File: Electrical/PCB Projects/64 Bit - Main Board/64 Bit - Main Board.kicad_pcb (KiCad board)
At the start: 4 copper layers, 200 x 100 mm, 242 parts, among them J1 61301021821, J10 M20-7920242R, J11 M20-7920242R, J12 M20-7920242R, J13 M20-7920242R, J14 1985195, J15 Conn_01x09, J16 Conn_01x09, J17 M20-7920242R, J18 M20-7920242R, J2 61301021821, J3 61301021821, J4 M20-7920242R, J5 USBC, J6 M20-7920242R, J7 PJ-102A, J8 M20-7920242R, J9 M20-7920242R, K1 JS-12N-K, K2 JS-12N-K, K3 JS-12N-K, K4 PR30-5V-450-1A-E, K5 PR30-12V-450-1A-E, P1 Conn_01x02, Q1 2N7002, Q10 XP231P0201TR-G, Q11 2N7002, Q2 XP231P0201TR-G, Q3 2N7002, Q4 2N7002, Q5 2N7002, Q6 XP231P0201TR-G, Q7 XP231P0201TR-G, Q8 2N7002, Q9 2N7002, SW1 1985195, SW2 1985195, SW3 1985195, SW4 1985195, SW5 L102011MS02Q, SW6 power_switch, U1 STM32F446RETx, U2 PCA9306, U3 DS1307+, U4 74HC3G34DC, U5 74HC3G34DC, U6 74HC3G34DC, U7 EN12-VS20AF20, U8 24LC64, U9 ESP32-C6-LCD-1.47, Y1 Crystal_GND24, Y2 32.768kHz-12.6pF, Y3 32.768kHz-12.6pF

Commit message: small pcb layout work
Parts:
- D47: moved to B.Cu
- moved JP1 67.8 mm to (191.9, 106.9), turned to -90 degrees
- moved D47 55.7 mm to (187.3, 103.5), turned to 180 degrees
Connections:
- D47 pad 2: Net-(D47-A) -> +5V
- JP1 pad 1: Net-(D47-A) -> Net-(JP1-A)
- JP1 pad 2: +5V -> Net-(D47-K)
- U9 pad 1: Net-(D47-K) -> Net-(JP1-A)
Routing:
- net encoder_button: track 196.4 -> 103.3 mm
- net encoder_A: track 215.8 -> 123.4 mm
- net encoder_B: track 227.6 -> 136.2 mm
- net +3V3: track 184.3 -> 103.8 mm, vias 17 -> 16
- net USART3_TX: track 164.4 -> 84.0 mm, vias 1 -> 0
- net IO9: track 152.6 -> 85.5 mm, vias 1 -> 0
- net USART3_RX: track 152.6 -> 86.8 mm, vias 1 -> 0
- net IO8: track 148.3 -> 84.8 mm
- net IO7: track 149.1 -> 86.8 mm
- net IO6: track 150.9 -> 89.0 mm
- net (no net): track 24.8 -> 0.00 mm
- net hv_output_relay: track 45.4 -> 32.0 mm
- net GND: vias 355 -> 332
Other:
- board text removed: "3v3"
- board text removed: "BL"
- board text removed: "CS"
- board text removed: "DC"
- board text removed: "MOSI"
- board text removed: "RST"
- board text removed: "SCK"
- board text removed: "SPI LCD"
- board text removed: "bottom"

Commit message: finished routing - added photoresistor to analog pin. Updated STM32Cube setup. Final stages of hardware design
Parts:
- removed D44, D45: TVS_0603, Resistor_SMD:R_0603_1608Metric
- removed the TP1 at (133.1, 160.6)
- removed the TP2 at (133.1, 164.1)
- removed the TP3 at (136.7, 160.6)
- removed the TP4 at (136.7, 164.1)
- removed the TP5 at (140.2, 160.6)
- removed the TP6 at (140.2, 164.1)
- added R80: R_Photo, OptoDevice:R_LDR_5.1x4.3mm_P3.4mm_Vertical, F.Cu at (76.5, 127.2)
- added R81: 10kohm_0603, Resistor_SMD:R_0603_1608Metric, F.Cu at (76.6, 121.0)
- D34, D35, D36, D37, D38, D39, D40, D41, D42, D43, D46, R76, R77, R78, R79: moved to B.Cu
- moved D36 134.5 mm to (84.2, 46.2), turned to 180 degrees
- moved D38 132.1 mm to (62.3, 74.7)
- moved D37 127.6 mm to (63.4, 78.1)
- moved D46 83.8 mm to (95.0, 122.5), turned to 90 degrees
- moved D43 75.5 mm to (94.8, 136.3), turned to 180 degrees
- moved D41 54.9 mm to (119.8, 133.9)
- moved D40 54.5 mm to (119.8, 132.1)
- moved D39 51.0 mm to (119.8, 135.7)
- moved R78 49.6 mm to (196.9, 134.7), turned to -90 degrees
- moved R79 49.0 mm to (193.9, 134.7), turned to -90 degrees
- moved R77 46.9 mm to (195.4, 134.7), turned to -90 degrees
- moved D35 45.9 mm to (196.2, 132.4), turned to 180 degrees
- moved D42 43.9 mm to (129.8, 132.0), turned to 90 degrees
- moved R76 43.0 mm to (192.4, 134.7), turned to -90 degrees
- moved D34 41.9 mm to (193.1, 132.4)
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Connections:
- U1 pad 8: unconnected-(U1-PC0-Pad8) -> photoResistor
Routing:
- net encoder_button: track 103.3 -> 201.7 mm
- net encoder_A: track 123.4 -> 221.0 mm
- net encoder_B: track 136.2 -> 232.4 mm
- net +3V3: track 103.8 -> 188.9 mm, vias 16 -> 17
- net USART3_TX: track 84.0 -> 147.7 mm, vias 0 -> 1
- net USART3_RX: track 86.8 -> 150.2 mm, vias 0 -> 1
- net +3V3_2: track 188.5 -> 224.2 mm
- net IO6: track 89.0 -> 66.2 mm, vias 0 -> 1
- net photoResistor: track 0.00 -> 18.3 mm, vias 0 -> 1
- net IO7: track 86.8 -> 70.4 mm, vias 0 -> 1
- net IO9: track 85.5 -> 101.2 mm, vias 0 -> 1
- net hv_output_relay: track 32.0 -> 45.4 mm
- net IO8: track 84.8 -> 72.2 mm, vias 0 -> 1
- net GND: track 160.1 -> 171.4 mm, vias 332 -> 520
- net +5V: track 405.6 -> 416.1 mm, vias 23 -> 24
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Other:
- board text added: "'64 Bit' Nixie Tube Clock Driver Board_V1.0 Nov 2025"
- board text removed: "'64 Bit' Nixie Tube Clock Driver Board_V1.0 Oct 2025"
- board text removed: "top"

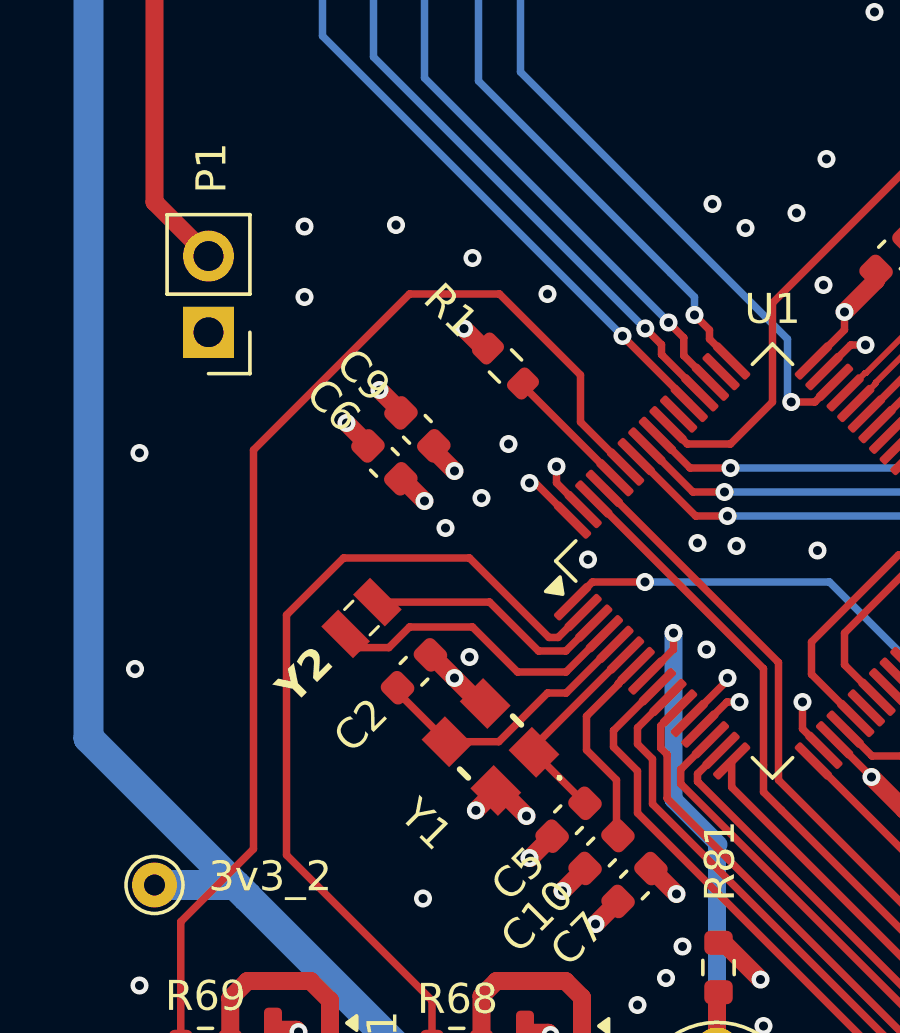
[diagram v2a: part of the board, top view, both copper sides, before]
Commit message: added I2C ambient light sensor
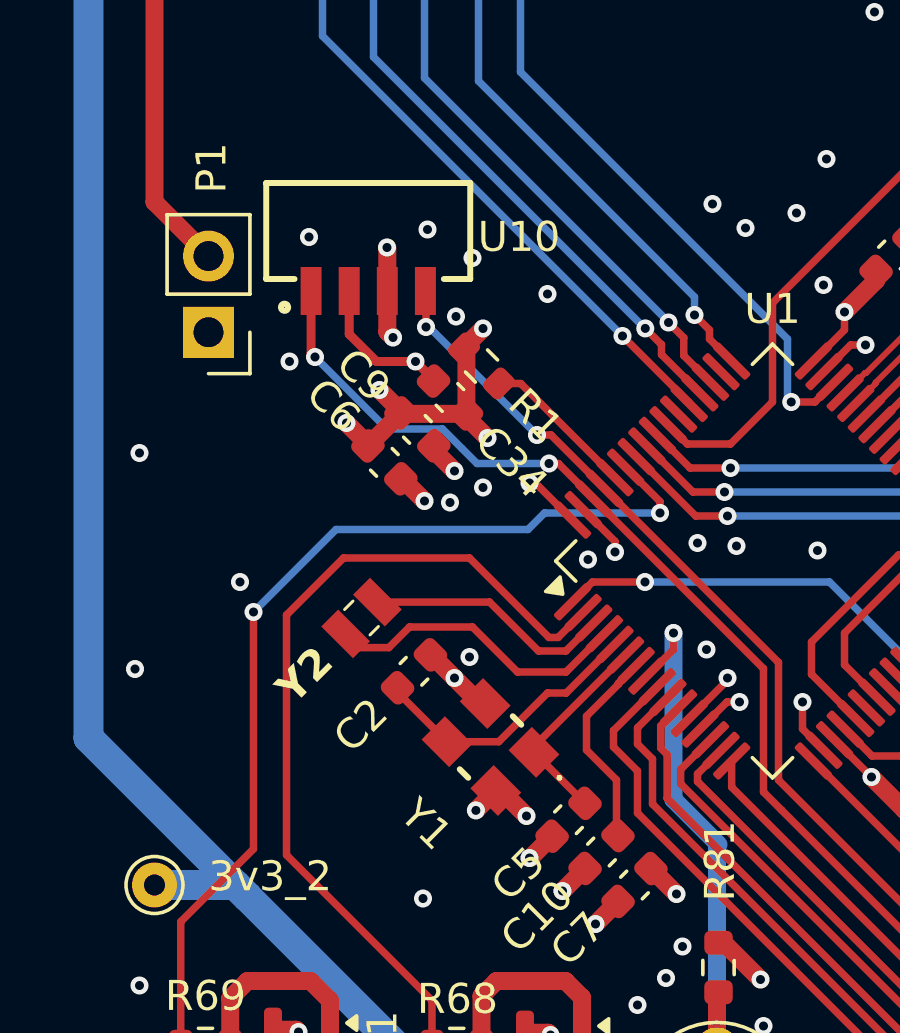
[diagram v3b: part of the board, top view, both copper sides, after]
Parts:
- added C34: 0.1uF_0603, Capacitor_SMD:C_0603_1608Metric, F.Cu at (67.7, 102.0)
- added U10: VEML7700-TR, Footprint drive Dump 1:VEML7700, F.Cu at (61.5, 98.1)
- moved R1 0.80 mm to (68.7, 101.0)
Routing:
- net SDA_3.3V: track 45.7 -> 59.2 mm, vias 0 -> 2
- net GND: track 171.4 -> 181.5 mm, vias 520 -> 524
- net SCL_3.3V: track 38.7 -> 48.1 mm, vias 0 -> 2
- net IO5: track 40.2 -> 33.8 mm, vias 0 -> 2
- net +3V3: track 188.9 -> 193.8 mm, vias 17 -> 18
- net Net-(U1-BOOT0): track 4.41 -> 5.17 mm
